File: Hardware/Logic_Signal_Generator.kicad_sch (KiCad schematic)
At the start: 0 parts

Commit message: [Hardware] Added the microcontroller and the supporting hardware to the schematic.
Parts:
- added C1, C3, C5: 100n, Capacitor_SMD:C_0603_1608Metric_Pad1.08x0.95mm_HandSolder, symbol Device:C
- added C2: 2.2u, Capacitor_SMD:C_0805_2012Metric_Pad1.18x1.45mm_HandSolder, symbol Device:C
- added C4: 470n, Capacitor_SMD:C_0603_1608Metric_Pad1.08x0.95mm_HandSolder, symbol Device:C
- added J1: JTAG, Connector_PinHeader_2.54mm:PinHeader_1x05_P2.54mm_Horizontal, symbol Connector_Generic:Conn_01x05
- added R1: 220, Resistor_SMD:R_0603_1608Metric_Pad0.98x0.95mm_HandSolder, symbol Device:R
- added R2: 10K, Resistor_SMD:R_0603_1608Metric_Pad0.98x0.95mm_HandSolder, symbol Device:R
- added U1: PIC18F25K50-xSO, Package_SO:SOIC-28W_7.5x17.9mm_P1.27mm, symbol MCU_Microchip_PIC18:PIC18F25K50-xSO
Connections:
- new net: C3.1, J1.5 (Pin_5), R1.1, R2.1
- new net: C4.1, C5.1, U1.14 (VUSB3V3/VDDCORE)
- new net: J1.1 (Pin_1), U1.27 (RB6/PGC)
- new net: J1.2 (Pin_2), U1.28 (RB7/PGD)
- new net +3.3V: C1.1, C2.1, J1.4 (Pin_4), R2.2, U1.20 (VDD)
- new net GND: C1.2, C2.2, C3.2, C4.2, C5.2, J1.3 (Pin_3), U1.19 (VSS), U1.8 (VSS)
- new net USB_D+: U1.16 (D+)
- new net USB_D-: U1.15 (D-)
- new net ~{MCLR}: R1.2, U1.1 (RE3/Vpp/~{MCLR})

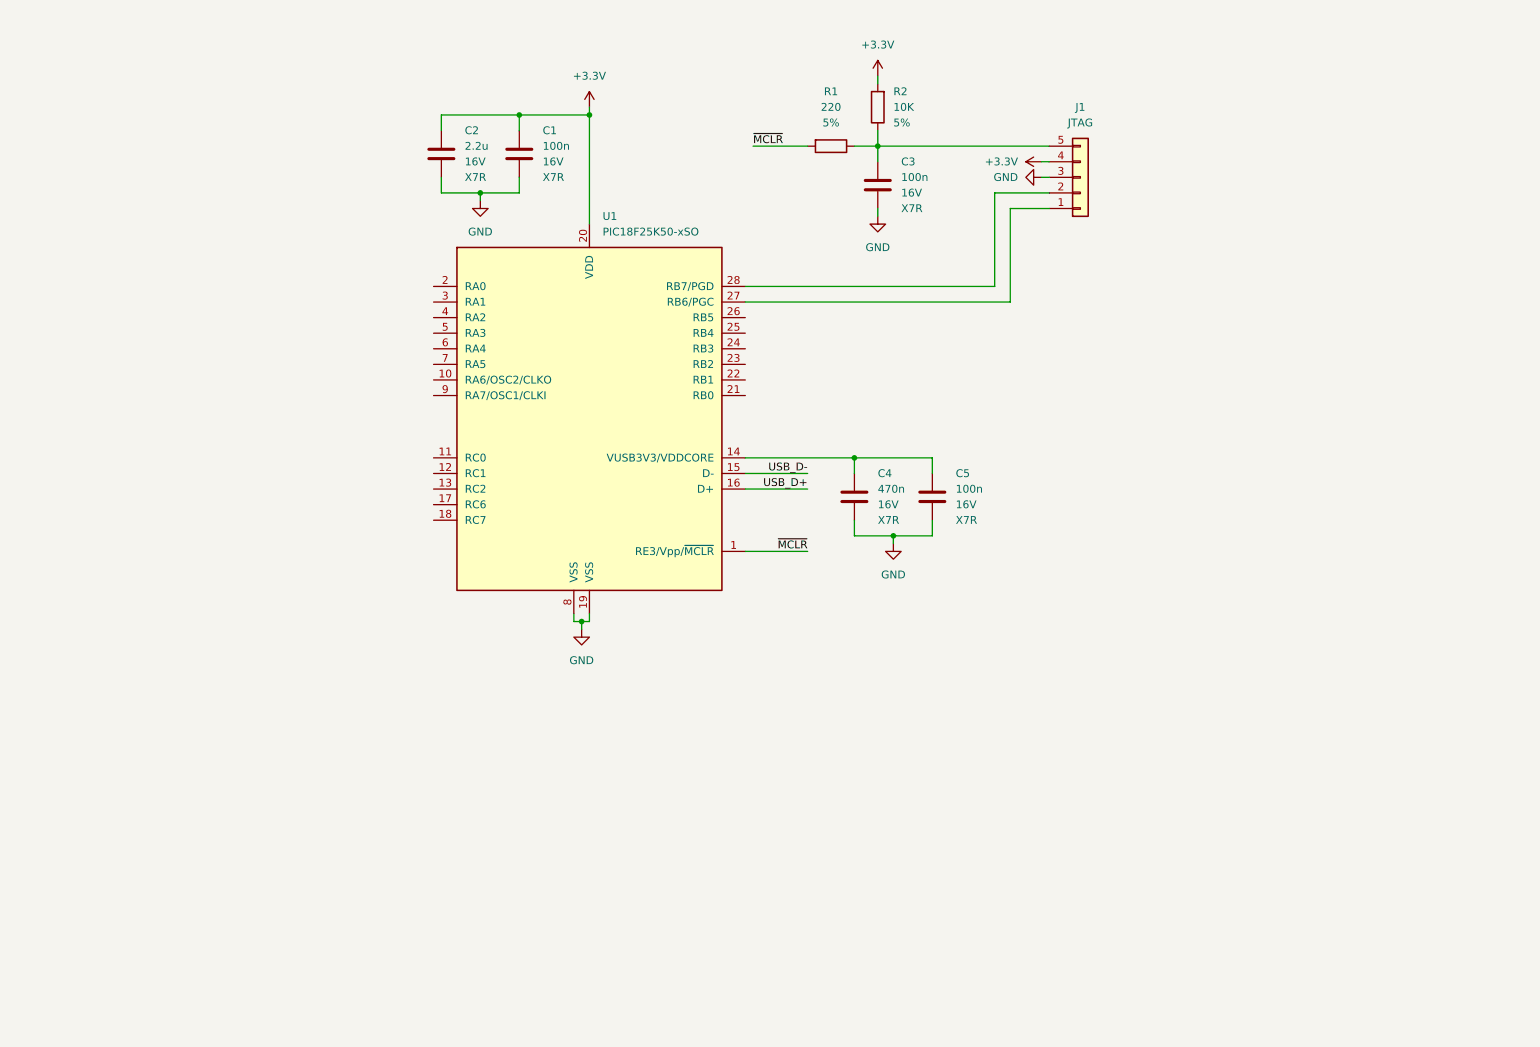
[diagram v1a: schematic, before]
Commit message: [Hardware] Added the voltage translator and the USB connector to the schematic.
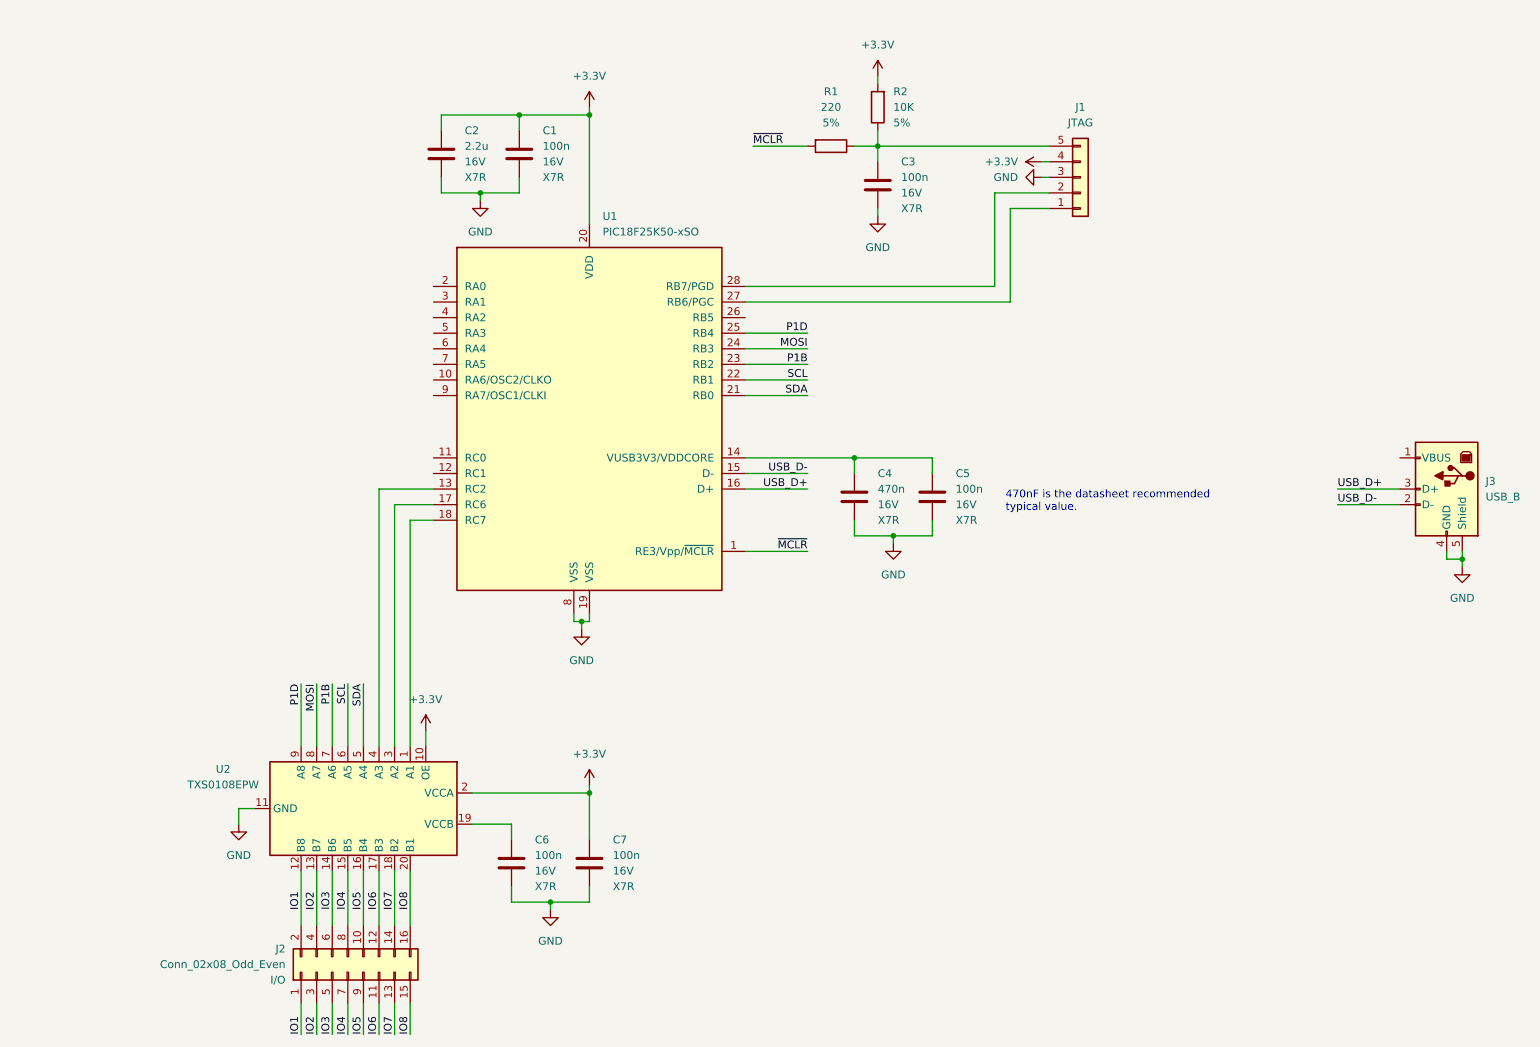
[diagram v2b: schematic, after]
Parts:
- added C6, C7: 100n, Capacitor_SMD:C_0603_1608Metric_Pad1.08x0.95mm_HandSolder, symbol Device:C
- added J2: Conn_02x08_Odd_Even, Connector_PinHeader_2.54mm:PinHeader_2x08_P2.54mm_Horizontal, symbol Connector_Generic:Conn_02x08_Odd_Even
- added J3: USB_B, Connector_USB:USB_B_Lumberg_2411_02_Horizontal, symbol Connector:USB_B
- added U2: TXS0108EPW, Package_SO:TSSOP-20_4.4x6.5mm_P0.65mm, symbol Logic_LevelTranslator:TXS0108EPW
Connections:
- net +3.3V: now also C7.1, U2.10 (OE), U2.2 (VCCA)
- net GND: now also C6.2, C7.2, J3.4 (GND), J3.5 (Shield), U2.11 (GND)
- net USB_D+: now also J3.3 (D+)
- net USB_D-: now also J3.2 (D-)
- net at U1.13 (RC2): now also U2.4 (A3)
- net at U1.17 (RC6): now also U2.3 (A2)
- net at U1.18 (RC7): now also U2.1 (A1)
- net SDA: now reaches U1.21 (RB0)
- net SDA: now also U2.5 (A4)
- net SCL: now reaches U1.22 (RB1)
- net SCL: now also U2.6 (A5)
- net P1B: now reaches U1.23 (RB2)
- net P1B: now also U2.7 (A6)
- net MOSI: now reaches U1.24 (RB3)
- net MOSI: now also U2.8 (A7)
- net P1D: now reaches U1.25 (RB4)
- net P1D: now also U2.9 (A8)
- new net: C6.1, U2.19 (VCCB)
- new net IO1: J2.1 (Pin_1), J2.2 (Pin_2), U2.12 (B8)
- new net IO2: J2.3 (Pin_3), J2.4 (Pin_4), U2.13 (B7)
- new net IO3: J2.5 (Pin_5), J2.6 (Pin_6), U2.14 (B6)
- new net IO4: J2.7 (Pin_7), J2.8 (Pin_8), U2.15 (B5)
- new net IO5: J2.10 (Pin_10), J2.9 (Pin_9), U2.16 (B4)
- new net IO6: J2.11 (Pin_11), J2.12 (Pin_12), U2.17 (B3)
- new net IO7: J2.13 (Pin_13), J2.14 (Pin_14), U2.18 (B2)
- new net IO8: J2.15 (Pin_15), J2.16 (Pin_16), U2.20 (B1)
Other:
- note added: "470nF is the datasheet recommended typical value."

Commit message: [Hardware] Added to the schematic the two LDOs to generate the +3.3V and +1.8V voltages.
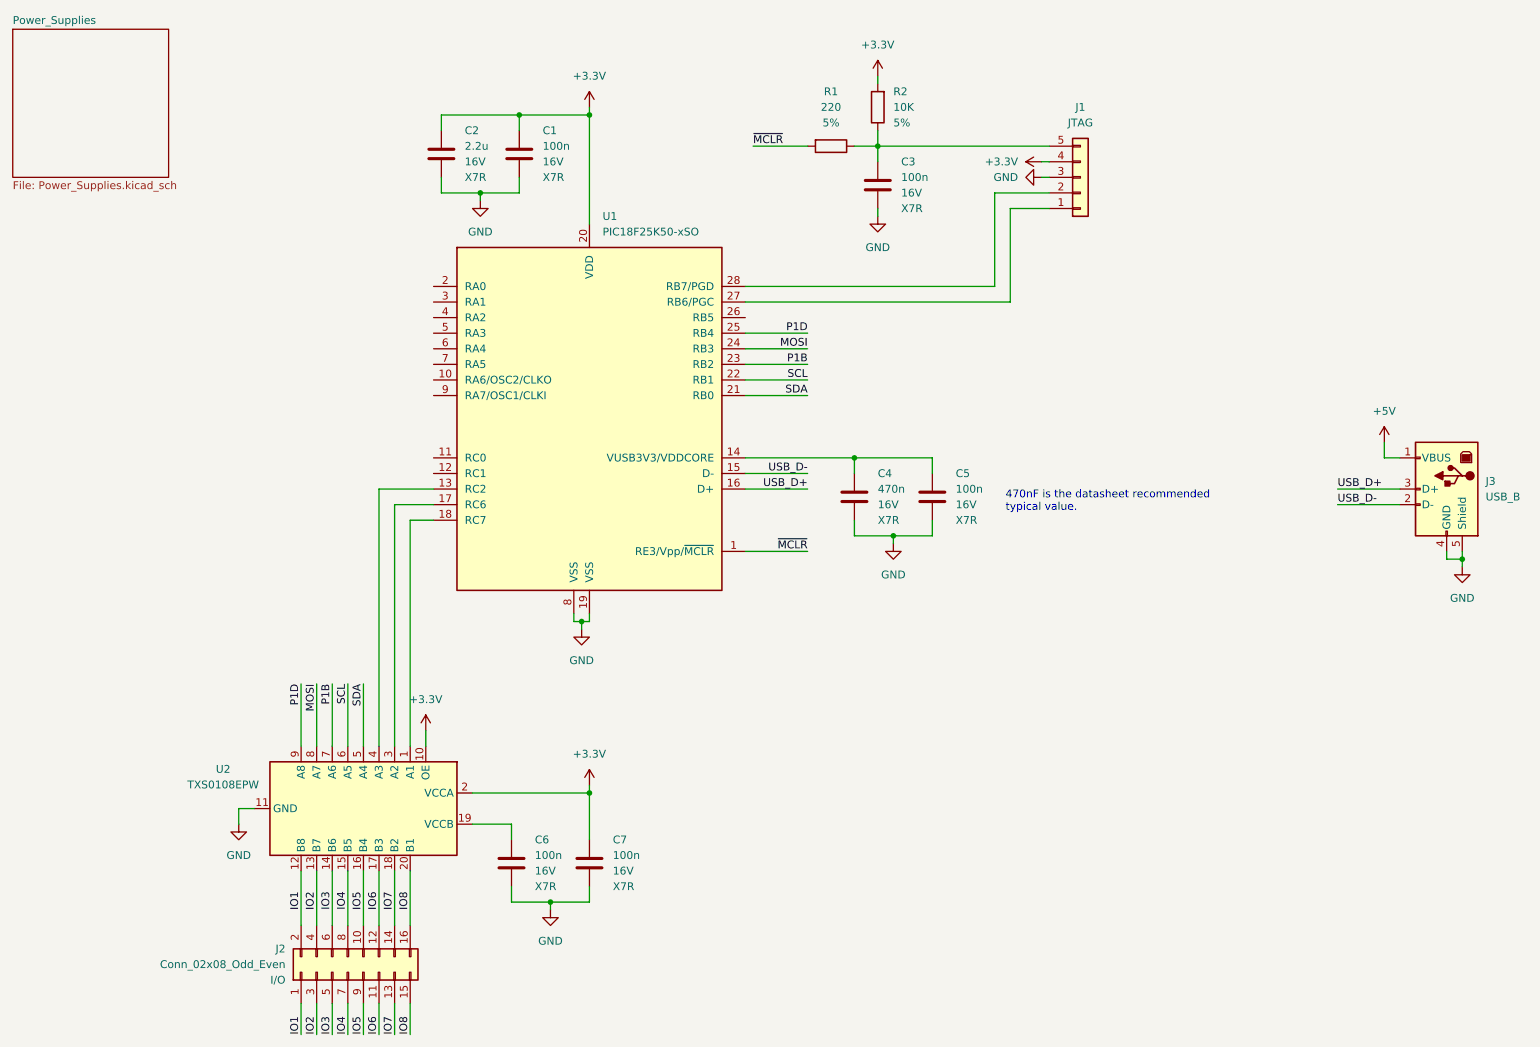
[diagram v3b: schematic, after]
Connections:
- net +5V: now reaches J3.1 (VBUS)
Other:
- added sheet Power_Supplies (Power_Supplies.kicad_sch)
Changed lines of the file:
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@@
+	(wire
+		(pts
+			(xy 248.92 92.71) (xy 248.92 95.25)
+		)
+		(stroke
+			(width 0)
+			(type default)
+		)
+	)
 	(wire
 		(pts
@@
 		(pts
 			(xy 261.62 111.76) (xy 261.62 110.49)
+		)
+		(stroke
+			(width 0)
+			(type default)
+		)
+	)
+	(wire
+		(pts
+			(xy 248.92 95.25) (xy 251.46 95.25)
 		)
 		(stroke
@@
 				(path "/24489a00-9deb-415a-805c-b5419253b078"
 					(reference "R1")
+					(unit 1)
+				)
+			)
+		)
+	)
+	(symbol
+		(lib_id "power:+5V")
+		(at 248.92 92.71 0)
+		(unit 1)
+		(exclude_from_sim no)
+		(in_bom yes)
+		(on_board yes)
+		(dnp no)
+		(fields_autoplaced yes)
+		(property "Reference" "#PWR012"
+			(at 248.92 96.52 0)
+			(effects
+				(font
+					(size 1.27 1.27)
+				)
+				(hide yes)
+			)
+		)
+		(property "Value" "+5V"
+			(at 248.92 87.63 0)
+			(effects
+				(font
+					(size 1.27 1.27)
+				)
+			)
+		)
+		(property "Footprint" ""
+			(at 248.92 92.71 0)
+			(effects
+				(font
+					(size 1.27 1.27)
+				)
+				(hide yes)
+			)
+		)
+		(property "Datasheet" ""
+			(at 248.92 92.71 0)
+			(effects
+				(font
+					(size 1.27 1.27)
+				)
+				(hide yes)
+			)
+		)
+		(property "Description" "Power symbol creates a global label with name \"+5V\""
+			(at 248.92 92.71 0)
+			(effects
+				(font
+					(size 1.27 1.27)
+				)
+				(hide yes)
+			)
+		)
+		(pin "1"
+		)
+		(instances
+			(project "Logic_Signal_Generator"
+				(path "/24489a00-9deb-415a-805c-b5419253b078"
+					(reference "#PWR012")
 					(unit 1)
 				)
@@
 				)
 			)
+		)
+	)
+	(sheet
+		(at 25.4 25.4)
+		(size 25.4 24.13)
+		(exclude_from_sim no)
+		(in_bom yes)
+		(on_board yes)
+		(dnp no)
+		(fields_autoplaced yes)
+		(stroke
+			(width 0.1524)
+			(type solid)
+		)
+		(fill
+			(color 0 0 0 0.0000)
+		)
+		(property "Sheetname" "Power_Supplies"
+			(at 25.4 24.6884 0)
+			(effects
+				(font
+					(size 1.27 1.27)
+				)
+				(justify left bottom)
+			)
+		)
+		(property "Sheetfile" "Power_Supplies.kicad_sch"
+			(at 25.4 50.1146 0)
+			(effects
+				(font
+					(size 1.27 1.27)
+				)
+				(justify left top)
+			)
+		)
+		(instances
+			(project "Logic_Signal_Generator"
+				(path "/24489a00-9deb-415a-805c-b5419253b078"
+					(page "2")
+				)
+			)

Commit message: [Hardware] Replaced the TXS0108E voltage shifter by discrete N-MOSFET transistors.
The TXS0108E was not working well during prototyping, it had difficulties determining the direction of the data transfer.

The microcontroller power supply has been switched from +3.3V to +5V to always provide the highest supported voltage on the N-MOSFET drain.
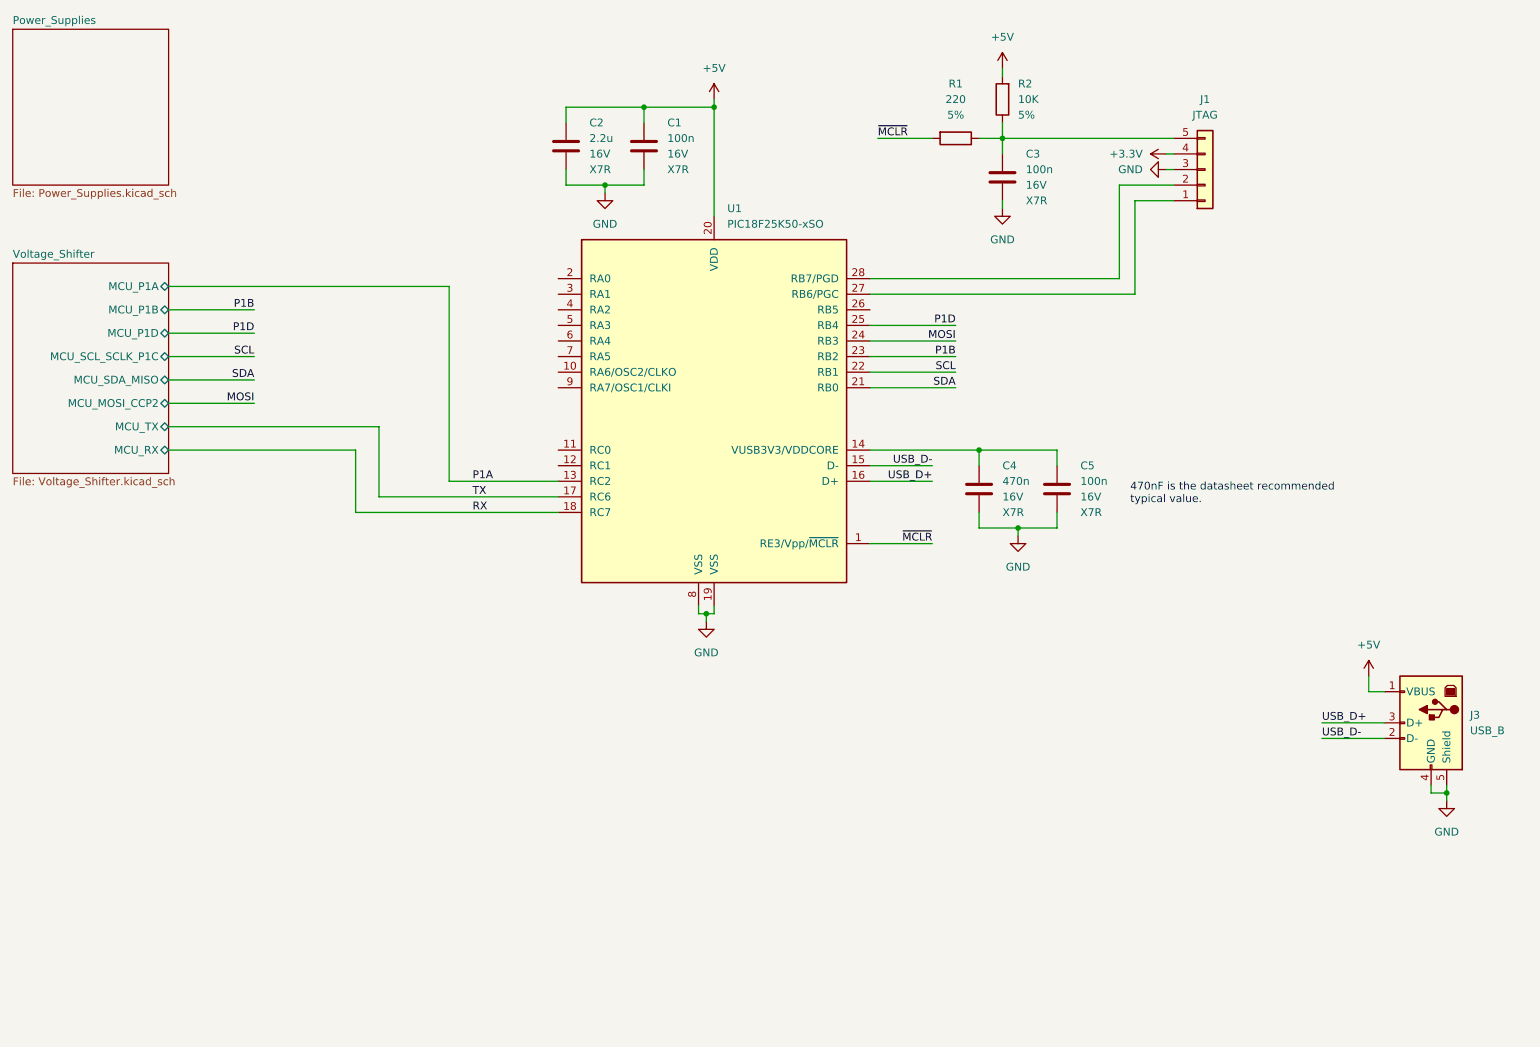
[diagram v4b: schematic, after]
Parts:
- removed C6, C7: 100n, Capacitor_SMD:C_0603_1608Metric_Pad1.08x0.95mm_HandSolder, symbol Device:C
- removed J2: Conn_02x08_Odd_Even, Connector_PinHeader_2.54mm:PinHeader_2x08_P2.54mm_Horizontal, symbol Connector_Generic:Conn_02x08_Odd_Even
- removed U2: TXS0108EPW, Package_SO:TSSOP-20_4.4x6.5mm_P0.65mm, symbol Logic_LevelTranslator:TXS0108EPW
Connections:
- net +3.3V: no longer C1.1, C2.1, R2.2, U1.20 (VDD)
- net +5V: now also C1.1, C2.1, R2.2, U1.20 (VDD)
- net P1A: now reaches U1.13 (RC2)
- net TX: now reaches U1.17 (RC6)
- net RX: now reaches U1.18 (RC7)
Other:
- added sheet Voltage_Shifter (Voltage_Shifter.kicad_sch)
- moved on the sheet: C1, C2, C3, C4, C5, J1, J3, R1, R2, U1
